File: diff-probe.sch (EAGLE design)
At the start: 133 parts, among them IC1 THS4721, IC11 LMH6702, IC2 OPA2130U, IC3 LMH6702, IC4 LMH6702, IC5 LMH6702, IC7 THS4721, J1 HEADER-1X2CARD-EDGE, J10 HEADER-1X2CARD-EDGE, J2 CON-1X3-TAB-AMP-29173-3-NARROW, J3 HEADER-1X2CARD-EDGE, J4 CON-1X3-TAB-AMP-29173-3-NARROW, J5 CON-1X3-TAB-AMP-29173-3-NARROW, J6 HEADER-1X2CARD-EDGE, J9 CON-1X3-TAB-AMP-29173-3-NARROW, U1 LMH6552, X1 SMA--BU-SMA-H, X2 SMA--BU-SMA-H, X3 SMA--BU-SMA-H, X4 SMA-142-0711-821/826, X5 SMA--BU-SMA-H

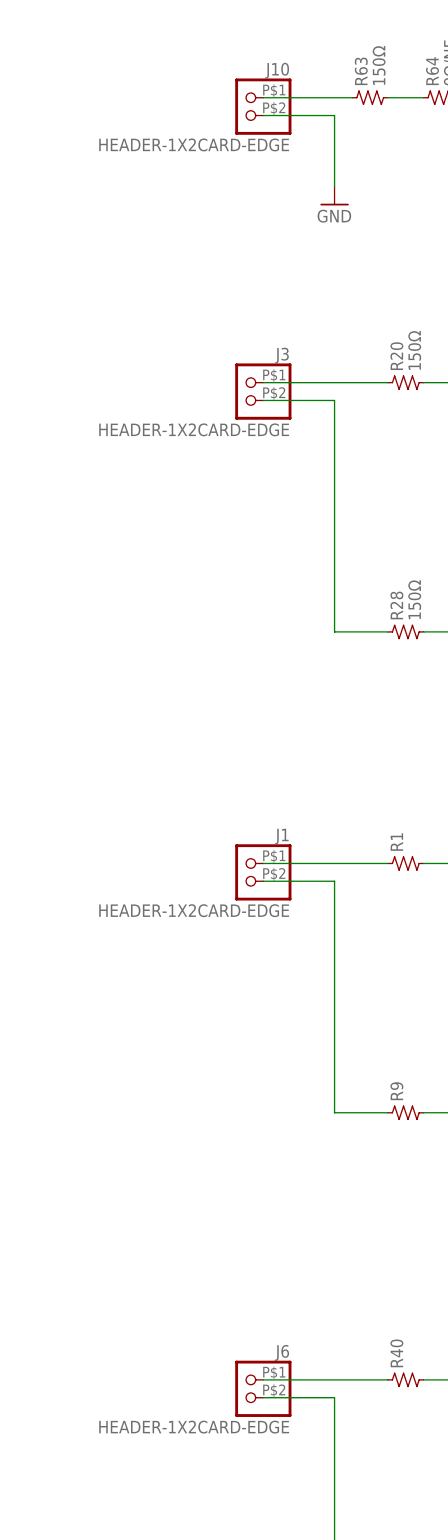
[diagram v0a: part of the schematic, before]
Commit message: Add "Variant" text to schematics.
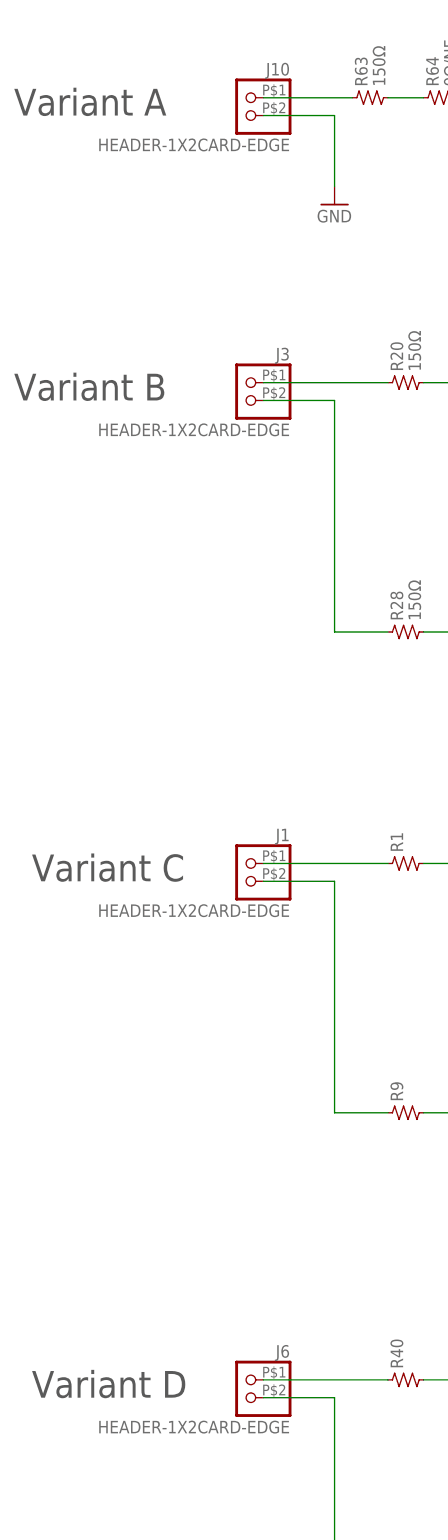
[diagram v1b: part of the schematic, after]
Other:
- note added: "Variant A"
- note added: "Variant B"
- note added: "Variant C"
- note added: "Variant D"
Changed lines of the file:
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@@
 <sheet>
 <plain>
+<text x="-5.08" y="248.92" size="3.81" layer="97">Variant A</text>
+<text x="-5.08" y="208.28" size="3.81" layer="97">Variant B</text>
+<text x="-2.54" y="139.7" size="3.81" layer="97">Variant C</text>
+<text x="-2.54" y="66.04" size="3.81" layer="97">Variant D</text>
 </plain>
 <instances>
